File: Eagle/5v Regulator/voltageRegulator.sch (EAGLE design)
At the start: 9 parts, among them U1 LM2576HVS-5.0/NOPB

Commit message: updated the regulator board
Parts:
- removed D1: BAT60J, diode:BAT60J
- added DIODE: 3000, rcl:R-EU_R1206
- C1: value 1000 uF -> 100 uF; device rcl:CPOL-EUB -> rcl:CPOL-EUE5-13
- C3: value 100 uF -> 1000 uF; device rcl:CPOL-EUB -> rcl:CPOL-EUE7.5-16
- L1: value 100 uH -> SFT1030; device rcl:L-EUL2012C -> inductors:SFT1030
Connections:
- net GND: now also DIODE.1, INPUT-1.S, OUTPUT-1.S, U1.TAB; no longer D1.A, INPUT-2.S, OUTPUT-2.S
- net LOAD+: now also C3.+, OUTPUT-2.S; no longer C1.+, OUTPUT-1.S
- net OUTPUT: now also DIODE.2; no longer D1.C
- net VCC: now also C1.+, INPUT-2.S; no longer C3.+, INPUT-1.S
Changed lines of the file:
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@@
 <parts>
 <part name="U1" library="IC" library_urn="urn:adsk.eagle:library:11396274" deviceset="LM2576HVS-5.0/NOPB" device="" package3d_urn="urn:adsk.eagle:package:10906047/2"/>
-<part name="D1" library="diode" library_urn="urn:adsk.eagle:library:210" deviceset="BAT60J" device="" package3d_urn="urn:adsk.eagle:package:43461/1"/>
-<part name="L1" library="rcl" library_urn="urn:adsk.eagle:library:334" deviceset="L-EU" device="L2012C" package3d_urn="urn:adsk.eagle:package:23475/2" value="100 uH"/>
 <part name="INPUT" library="con-molex" library_urn="urn:adsk.eagle:library:165" deviceset="22-23-2021" device="" package3d_urn="urn:adsk.eagle:package:8078633/1"/>
 <part name="OUTPUT" library="con-molex" library_urn="urn:adsk.eagle:library:165" deviceset="22-23-2021" device="" package3d_urn="urn:adsk.eagle:package:8078633/1"/>
@@
 <part name="SUPPLY6" library="supply2" library_urn="urn:adsk.eagle:library:372" deviceset="GND" device=""/>
 <part name="SUPPLY7" library="supply2" library_urn="urn:adsk.eagle:library:372" deviceset="GND" device=""/>
-<part name="C3" library="rcl" library_urn="urn:adsk.eagle:library:334" deviceset="CPOL-EU" device="B" package3d_urn="urn:adsk.eagle:package:23421/2" value="100 uF"/>
-<part name="C1" library="rcl" library_urn="urn:adsk.eagle:library:334" deviceset="CPOL-EU" device="B" package3d_urn="urn:adsk.eagle:package:23421/2" value="1000 uF"/>
+<part name="L1" library="inductors" library_urn="urn:adsk.eagle:library:243" deviceset="SFT1030" device="" package3d_urn="urn:adsk.eagle:package:15108/1"/>
+<part name="C3" library="rcl" library_urn="urn:adsk.eagle:library:334" deviceset="CPOL-EU" device="E7.5-16" package3d_urn="urn:adsk.eagle:package:23382/2" value="1000 uF"/>
+<part name="C1" library="rcl" library_urn="urn:adsk.eagle:library:334" deviceset="CPOL-EU" device="E5-13" package3d_urn="urn:adsk.eagle:package:23375/1" value="100 uF"/>
+<part name="DIODE" library="rcl" library_urn="urn:adsk.eagle:library:334" deviceset="R-EU_" device="R1206" package3d_urn="urn:adsk.eagle:package:23540/2" value="3000"/>
 </parts>
 <sheets>
@@
 <attribute name="VALUE" x="25.4" y="58.42" size="2.1844" layer="96"/>
 </instance>
-<instance part="D1" gate="G$1" x="27.94" y="35.56" smashed="yes" rot="R90">
-<attribute name="NAME" x="26.035" y="33.274" size="1.778" layer="95" rot="R90"/>
-</instance>
-<instance part="L1" gate="G$1" x="35.56" y="40.64" smashed="yes" rot="R90">
-<attribute name="VALUE" x="39.37" y="43.942" size="1.778" layer="96" rot="R180"/>
-</instance>
-<instance part="INPUT" gate="-1" x="73.66" y="86.36" smashed="yes" rot="R90"/>
-<instance part="INPUT" gate="-2" x="78.74" y="86.36" smashed="yes" rot="R90"/>
-<instance part="OUTPUT" gate="-1" x="116.84" y="76.2" smashed="yes"/>
-<instance part="OUTPUT" gate="-2" x="116.84" y="73.66" smashed="yes"/>
+<instance part="INPUT" gate="-1" x="73.66" y="88.9" smashed="yes" rot="R90"/>
+<instance part="INPUT" gate="-2" x="78.74" y="88.9" smashed="yes" rot="R90"/>
+<instance part="OUTPUT" gate="-1" x="91.44" y="88.9" smashed="yes" rot="R90"/>
+<instance part="OUTPUT" gate="-2" x="96.52" y="88.9" smashed="yes" rot="R90"/>
 <instance part="R1" gate="G$1" x="55.88" y="20.32" smashed="yes" rot="R90">
 <attribute name="NAME" x="54.3814" y="16.51" size="1.778" layer="95" rot="R90"/>
@@
 <attribute name="VALUE" x="59.182" y="31.75" size="1.778" layer="96" rot="R90"/>
 </instance>
-<instance part="SUPPLY1" gate="GND" x="78.74" y="81.28" smashed="yes">
-<attribute name="VALUE" x="81.915" y="83.185" size="1.778" layer="96"/>
+<instance part="SUPPLY1" gate="GND" x="73.66" y="83.82" smashed="yes">
+<attribute name="VALUE" x="66.675" y="85.725" size="1.778" layer="96"/>
 </instance>
-<instance part="SUPPLY2" gate="G$1" x="73.66" y="81.28" smashed="yes" rot="R180">
-<attribute name="VALUE" x="70.485" y="83.185" size="1.778" layer="96" rot="R180"/>
+<instance part="SUPPLY2" gate="G$1" x="78.74" y="83.82" smashed="yes" rot="R180">
+<attribute name="VALUE" x="85.725" y="88.265" size="1.778" layer="96" rot="R180"/>
 </instance>
 <instance part="SUPPLY3" gate="GND" x="12.7" y="63.5" smashed="yes">
@@
 <attribute name="VALUE" x="28.575" y="29.845" size="1.778" layer="96"/>
 </instance>
-<instance part="SUPPLY6" gate="GND" x="111.76" y="73.66" smashed="yes" rot="R270">
-<attribute name="VALUE" x="113.665" y="70.485" size="1.778" layer="96" rot="R270"/>
+<instance part="SUPPLY6" gate="GND" x="91.44" y="81.28" smashed="yes">
+<attribute name="VALUE" x="84.455" y="83.185" size="1.778" layer="96"/>
 </instance>
 <instance part="SUPPLY7" gate="GND" x="53.34" y="71.12" smashed="yes" rot="R90"/>
-<instance part="C3" gate="G$1" x="12.7" y="73.66" smashed="yes">
-<attribute name="VALUE" x="3.683" y="74.1426" size="1.778" layer="96"/>
+<instance part="L1" gate="G$1" x="35.56" y="40.64" smashed="yes">
+<attribute name="NAME" x="31.75" y="42.926" size="1.778" layer="95"/>
+<attribute name="VALUE" x="31.623" y="37.592" size="1.778" layer="96"/>
 </instance>
-<instance part="C1" gate="G$1" x="43.18" y="38.1" smashed="yes">
-<attribute name="VALUE" x="39.243" y="30.9626" size="1.778" layer="96"/>
+<instance part="C3" gate="G$1" x="43.18" y="38.1" smashed="yes">
+<attribute name="VALUE" x="44.323" y="33.5026" size="1.778" layer="96"/>
+</instance>
+<instance part="C1" gate="G$1" x="12.7" y="73.66" smashed="yes">
+<attribute name="VALUE" x="13.843" y="69.0626" size="1.778" layer="96"/>
+</instance>
+<instance part="DIODE" gate="G$1" x="25.4" y="35.56" smashed="yes" rot="R90">
+<attribute name="NAME" x="23.9014" y="31.75" size="1.778" layer="95" rot="R90"/>
 </instance>
 </instances>
@@
 <net name="VCC" class="0">
 <segment>
-<pinref part="INPUT" gate="-1" pin="S"/>
-<pinref part="SUPPLY2" gate="G$1" pin="VCC"/>
-</segment>
-<segment>
 <pinref part="U1" gate="G$1" pin="VIN"/>
 <wire x1="12.7" y1="76.2" x2="20.32" y2="76.2" width="0.1524" layer="91"/>
 <label x="12.7" y="78.74" size="1.778" layer="95" rot="R90" xref="yes"/>
 <wire x1="12.7" y1="78.74" x2="12.7" y2="76.2" width="0.1524" layer="91"/>
-<pinref part="C3" gate="G$1" pin="+"/>
+<pinref part="C1" gate="G$1" pin="+"/>
 <junction x="12.7" y="76.2"/>
+</segment>
+<segment>
+<pinref part="INPUT" gate="-2" pin="S"/>
+<pinref part="SUPPLY2" gate="G$1" pin="VCC"/>
 </segment>
 </net>
 <net name="GND" class="0">
-<segment>
-<pinref part="INPUT" gate="-2" pin="S"/>
-<pinref part="SUPPLY1" gate="GND" pin="GND"/>
-</segment>
 <segment>
 <pinref part="U1" gate="G$1" pin="GND"/>
@@
 <pinref part="SUPPLY3" gate="GND" pin="GND"/>
 <junction x="12.7" y="66.04"/>
-<pinref part="C3" gate="G$1" pin="-"/>
-</segment>
-<segment>
-<pinref part="D1" gate="G$1" pin="A"/>
-<wire x1="43.18" y1="33.02" x2="35.56" y2="33.02" width="0.1524" layer="91"/>
-<wire x1="35.56" y1="33.02" x2="27.94" y2="33.02" width="0.1524" layer="91"/>
-<wire x1="35.56" y1="33.02" x2="35.56" y2="30.48" width="0.1524" layer="91"/>
-<pinref part="SUPPLY5" gate="GND" pin="GND"/>
 <pinref part="C1" gate="G$1" pin="-"/>
 </segment>
 <segment>
-<pinref part="OUTPUT" gate="-2" pin="S"/>
-<pinref part="SUPPLY6" gate="GND" pin="GND"/>
+<wire x1="35.56" y1="30.48" x2="25.4" y2="30.48" width="0.1524" layer="91"/>
+<pinref part="SUPPLY5" gate="GND" pin="GND"/>
+<pinref part="DIODE" gate="G$1" pin="1"/>
+<pinref part="C3" gate="G$1" pin="-"/>
+<wire x1="43.18" y1="33.02" x2="43.18" y2="30.48" width="0.1524" layer="91"/>
+<wire x1="43.18" y1="30.48" x2="35.56" y2="30.48" width="0.1524" layer="91"/>
 </segment>
 <segment>
@@
 <pinref part="SUPPLY4" gate="GND" pin="GND"/>
 </segment>
+<segment>
+<pinref part="U1" gate="G$1" pin="TAB"/>
+<wire x1="50.8" y1="76.2" x2="53.34" y2="76.2" width="0.1524" layer="91"/>
+<label x="53.34" y="76.2" size="1.778" layer="95" xref="yes"/>
+</segment>
+<segment>
+<pinref part="INPUT" gate="-1" pin="S"/>
+<pinref part="SUPPLY1" gate="GND" pin="GND"/>
+</segment>
+<segment>
+<pinref part="OUTPUT" gate="-1" pin="S"/>
+<pinref part="SUPPLY6" gate="GND" pin="GND"/>
+<wire x1="91.44" y1="83.82" x2="91.44" y2="86.36" width="0.1524" layer="91"/>
+</segment>
 </net>
 <net name="LOAD+" class="0">
 <segment>
-<pinref part="OUTPUT" gate="-1" pin="S"/>
-<wire x1="114.3" y1="76.2" x2="109.22" y2="76.2" width="0.1524" layer="91"/>
-<label x="109.22" y="76.2" size="1.778" layer="95" rot="R180" xref="yes"/>
-</segment>
-<segment>
-<pinref part="L1" gate="G$1" pin="2"/>
 <pinref part="R2" gate="G$1" pin="2"/>
 <wire x1="55.88" y1="40.64" x2="43.18" y2="40.64" width="0.1524" layer="91"/>
@@
 <wire x1="55.88" y1="40.64" x2="60.96" y2="40.64" width="0.1524" layer="91"/>
 <label x="60.96" y="40.64" size="1.778" layer="95" xref="yes"/>
-<pinref part="C1" gate="G$1" pin="+"/>
 <junction x="43.18" y="40.64"/>
+<pinref part="L1" gate="G$1" pin="2"/>
+<pinref part="C3" gate="G$1" pin="+"/>
+</segment>
+<segment>
+<pinref part="OUTPUT" gate="-2" pin="S"/>
+<wire x1="96.52" y1="86.36" x2="96.52" y2="83.82" width="0.1524" layer="91"/>
+<label x="96.52" y="83.82" size="1.778" layer="95" rot="R270" xref="yes"/>
 </segment>
 </net>
 <net name="OUTPUT" class="0">
 <segment>
+<wire x1="27.94" y1="40.64" x2="25.4" y2="40.64" width="0.1524" layer="91"/>
+<label x="22.86" y="40.64" size="1.778" layer="95" rot="R180" xref="yes"/>
 <pinref part="L1" gate="G$1" pin="1"/>
-<pinref part="D1" gate="G$1" pin="C"/>
-<wire x1="30.48" y1="40.64" x2="27.94" y2="40.64" width="0.1524" layer="91"/>
-<wire x1="27.94" y1="40.64" x2="27.94" y2="38.1" width="0.1524" layer="91"/>
-<wire x1="27.94" y1="40.64" x2="22.86" y2="40.64" width="0.1524" layer="91"/>
-<label x="22.86" y="40.64" size="1.778" layer="95" rot="R180" xref="yes"/>
+<pinref part="DIODE" gate="G$1" pin="2"/>
+<wire x1="25.4" y1="40.64" x2="22.86" y2="40.64" width="0.1524" layer="91"/>
+<junction x="25.4" y="40.64"/>
 </segment>
 <segment>

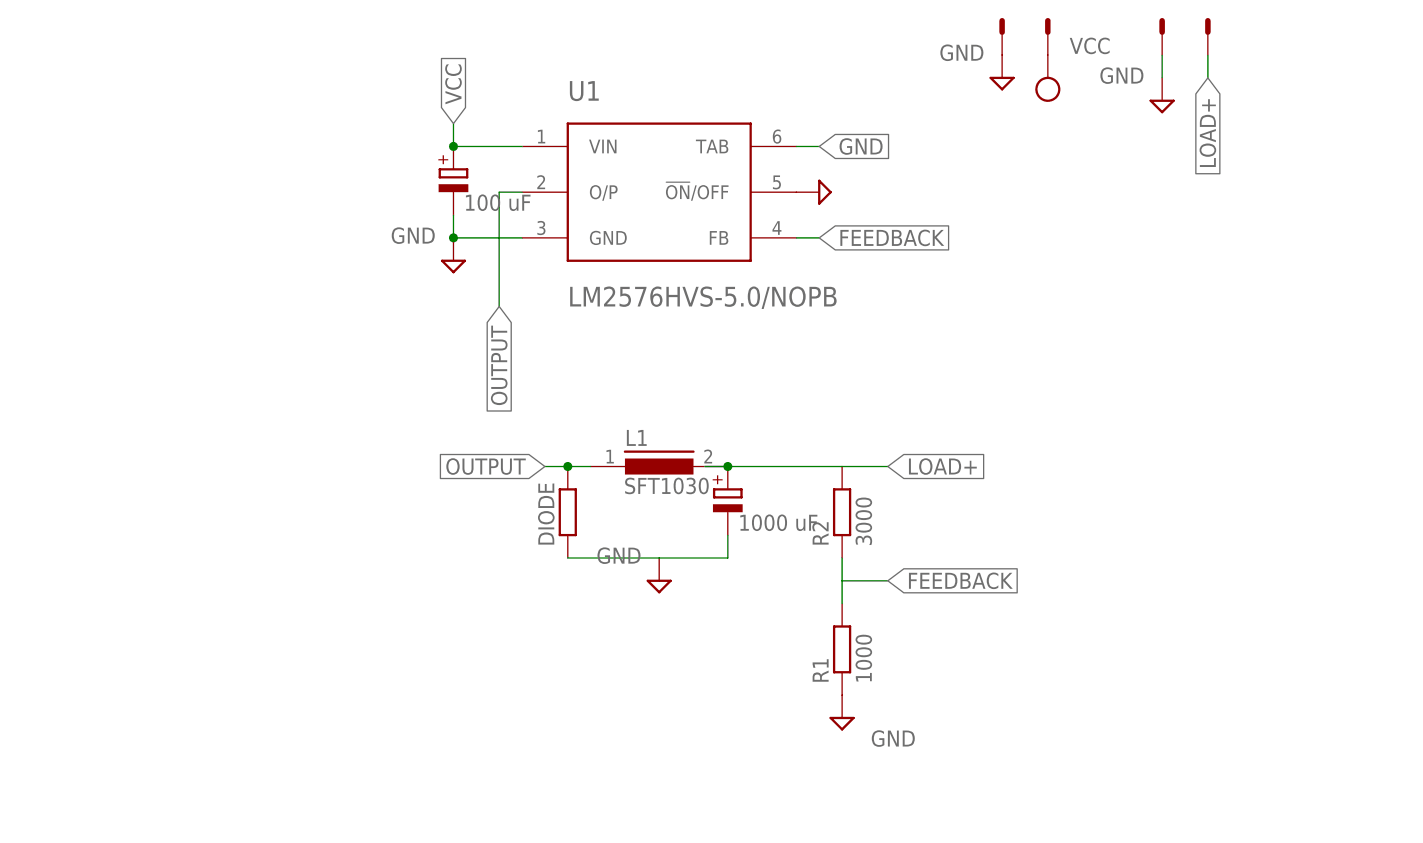
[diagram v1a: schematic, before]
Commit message: Updated the voltage regulator schematic
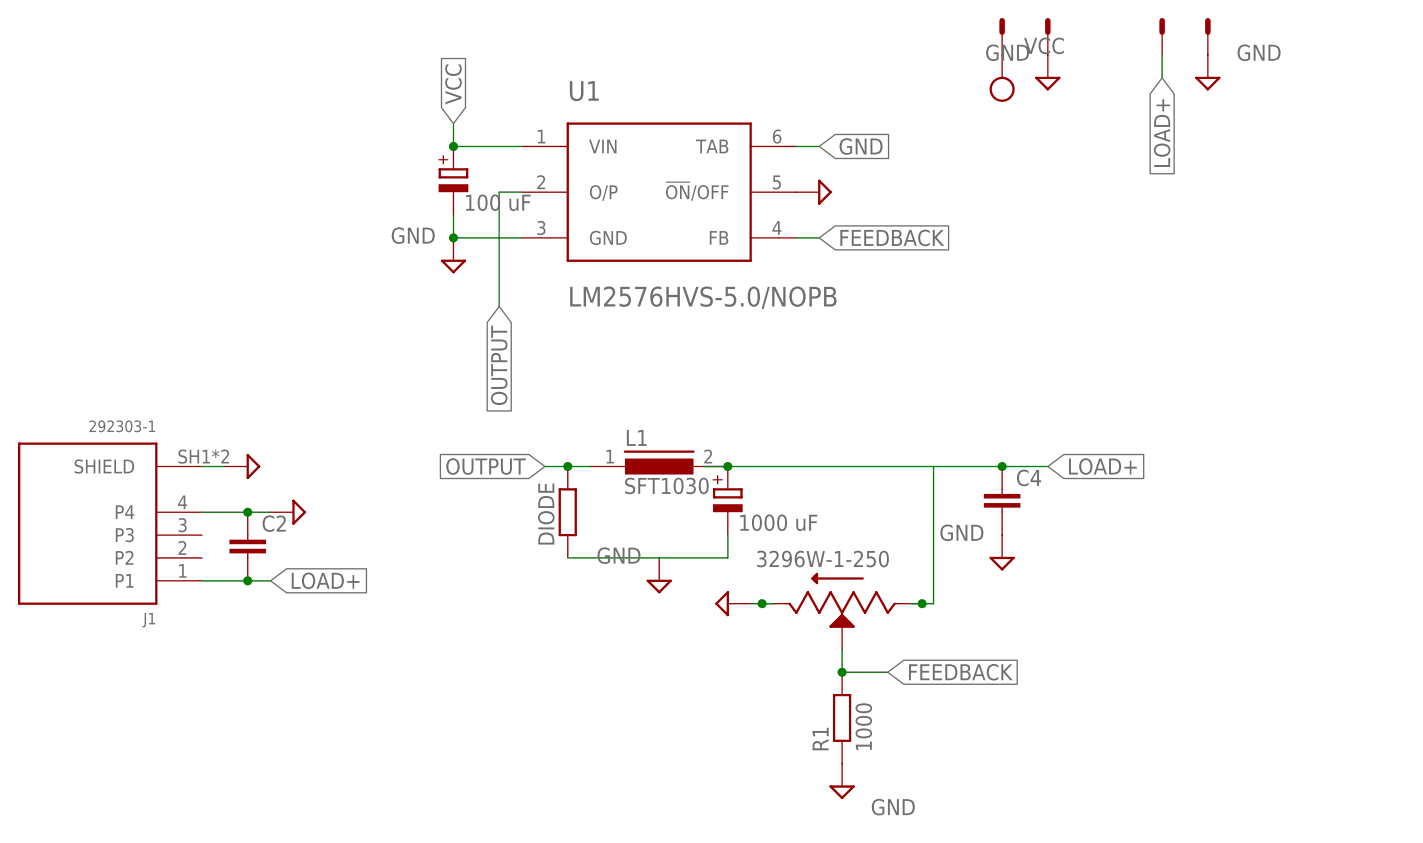
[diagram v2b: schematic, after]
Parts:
- removed R2: 3000, rcl:R-EU_R1206
- added C2, C4: (no value), rcl:C-EUC1206K
- added J1: 292303-1, 292303-1:292303-1
- added VR1: 3296W-1-250, 3296W-1-250:3296W-1-250
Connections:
- net FEEDBACK: now also VR1.WIPER; no longer R2.1
- net GND: now also C2.1, C4.2, INPUT-2.S, J1.P4, J1.SHIELD, OUTPUT-2.S, VR1.CW; no longer INPUT-1.S, OUTPUT-1.S
- net LOAD+: now also C2.2, C4.1, J1.P1, OUTPUT-1.S, VR1.CCW; no longer OUTPUT-2.S, R2.2
- net VCC: now also INPUT-1.S; no longer INPUT-2.S
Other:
- moved on the sheet: R1
